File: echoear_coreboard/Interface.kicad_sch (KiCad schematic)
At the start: 0 parts

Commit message: Starting Interface SCH
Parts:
- added U2: (no value), symbol Symbols:1.0K-N-3PB
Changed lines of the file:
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@@
 	(generator_version "10.0")
 	(paper "A4")
+	(symbol
+		(lib_id "Symbols:1.0K-N-3PB")
+		(at 34.29 29.21 0)
+		(unit 1)
+		(body_style 1)
+		(exclude_from_sim no)
+		(in_bom yes)
+		(on_board yes)
+		(in_pos_files yes)
+		(dnp no)
+		(fields_autoplaced yes)
+		(property "Reference" "U2"
+			(at 45.72 38.0999 0)
+			(show_name no)
+			(do_not_autoplace no)
+			(effects
+				(font
+					(size 1.27 1.27)
+				)
+				(justify left)
+			)
+		)
+		(property "Value" ""
+			(at 34.29 29.21 0)
+			(show_name no)
+			(do_not_autoplace no)
+			(effects
+				(font
+					(size 1.27 1.27)
+				)
+			)
+		)
+		(property "Footprint" ""
+			(at 34.29 29.21 0)
+			(hide yes)
+			(show_name no)
+			(do_not_autoplace no)
+			(effects
+				(font
+					(size 1.27 1.27)
+				)
+			)
+		)
+		(property "Datasheet" ""
+			(at 34.29 29.21 0)
+			(hide yes)
+			(show_name no)
+			(do_not_autoplace no)
+			(effects
+				(font
+					(size 1.27 1.27)
+				)
+			)
+		)
+		(property "Description" ""
+			(at 34.29 29.21 0)
+			(hide yes)
+			(show_name no)
+			(do_not_autoplace no)
+			(effects
+				(font
+					(size 1.27 1.27)
+				)
+			)
+		)
+		(pin ""
+		)
+		(pin ""
+		)
+		(pin ""
+		)
+		(pin ""
+		)
+		(pin ""
+		)
+		(instances
+			(project "echoear_coreboard"
+				(path "/919b249b-28e6-49d6-a46c-47b0cfe0d5d1/25b0c935-1253-4e1a-a7e3-572f314d3e73"
+					(reference "U2")
+					(unit 1)
+				)
+			)
+		)
+	)
 )

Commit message: Finished touch schematic
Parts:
- added CN1: HC-1.25-2PLT, Library:CONN-SMD_HC-1.25-2PLT, symbol Sym_easyeda2kicad:HC-1.25-2PLT
- U2: value (none) -> 1.0K-N-3PB; footprint (none) -> Library:FPC-SMD_3P-P1.00_HDGC_1.0K-N-3PB; LCSC (none) -> C2915549
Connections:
- net TOUCH: now reaches U2. (4)
- net TOUCH: now also CN1.1, CN1.2
- new net GND: CN1.3, CN1.4, U2. (4)
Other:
- note added: "TOUCH"
- moved on the sheet: U2

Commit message: First draft of Interface SCH
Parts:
- added C4: 10u, Capacitor_SMD:C_0603_1608Metric, symbol Device:C
- added C5, C6: 100n, Capacitor_SMD:C_0402_1005Metric, symbol Device:C
- added CN2: HC-1.25-2PLT, easyeda2kicad:CONN-SMD_HC-1.25-2PLT, symbol Sym_easyeda2kicad:HC-1.25-2PLT
- added CN3: YXT-BB10-24S-02, easyeda2kicad:CONN-SMD_YXT-BB10-24S-02, symbol Sym_easyeda2kicad:YXT-BB10-24S-02
- added H1, H2: ZX-PZ1.27-2-4PWZ, easyeda2kicad:HDR-SMD_8P-P1.27-LS5.5_ZX-PZ1.27-2-4PWZ, symbol Symbols:ZX-PZ1.27-2-4PWZ
- added Q1: AO3401A, Package_TO_SOT_SMD:SOT-23, symbol Transistor_FET:AO3401A
- added Q2: AO3400A, Package_TO_SOT_SMD:SOT-23, symbol Transistor_FET:AO3400A
- added R4: 20 ohms, Resistor_SMD:R_0402_1005Metric, symbol Device:R
- added R5: 10k, Resistor_SMD:R_0402_1005Metric, symbol Device:R
- added U2: 8.03A0.039200, easyeda2kicad:FPC-SMD_39P-P0.60_DIANWEI_8.03A0.039200, symbol Sym_easyeda2kicad:8.03A0.039200
- added U3: BMI270, easyeda2kicad:LGA-14_L3.0-W2.5-P0.50-BR, symbol Sym_easyeda2kicad:BMI270
- renumbered U2 to FPC1
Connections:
- net GND: now also C4.1, C5.1, C6.2, CN2.1, CN2.3, CN2.4, CN3.11, CN3.15, CN3.17, CN3.19, CN3.25, CN3.26, CN3.27, CN3.28, CN3.3, CN3.8, H1.1, Q2.2 (S), R5.2, U2.1, U2.20, U2.27, U2.30, U2.33, U2.36, U2.39, U2.40, U2.41, U2.7, U2.9, U3.1 (SDO), U3.6 (GNDIO), U3.7 (GND)
- new net: Q2.3 (D), R4.2
- new net BAT_SCL: H1.4
- new net BAT_SDA: H1.2
- new net CHIP_PU: H2.3
- new net ESP_BOOT: H1.8
- new net ICM_INT1: U3.4 (INT1)
- new net ICM_SCL: U3.13 (SCX)
- new net ICM_SDA: U3.14 (SDX)
- new net LCD_BLK: Q2.1 (G), R5.1
- new net LCD_CS: CN3.24, U2.11
- new net LCD_DC: U2.8
- new net LCD_RST: CN3.12, CN3.6, U2.21, U2.4
- new net LCD_SCL: CN3.21, U2.10
- new net LCD_SDA0: CN3.23, U2.12
- new net LCD_SDA1: CN3.22, U2.13
- new net LCD_SDA2: CN3.18, U2.14
- new net LCD_SDA3: CN3.16, U2.15
- new net LCD_TE: CN3.13, U2.22
- new net LEDK: CN3.2, U2.38
- new net LED_K: R4.1
- new net MCU_3V3: C5.2, C6.1, CN3.9, H1.5, Q1.2 (S), U2.2, U3.12 (CSB), U3.5 (VDDIO), U3.8 (VDD)
- new net POWER_CTRL: H1.7, Q1.1 (G)
- new net SD_CLK: H2.5
- new net SD_CMD: H1.6
- new net SD_DA0: H2.7
- new net TP_INT: CN3.7, U2.3
- new net TP_SCL: CN3.4, U2.6
- new net TP_SDA: CN3.5, U2.5
- new net U1RXD: H2.1
- new net U1TXD: H2.4
- new net USB_DN: H2.6
- new net USB_DP: H2.8
- new net VBAT_IN: CN2.2, H1.3
- new net VCC_3V3: C4.2, CN3.1, CN3.10, Q1.3 (D), U2.25, U2.26, U2.28, U2.29, U2.37
- new net VIN: H2.2
- no-connect marks 0 -> 17
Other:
- note added: "B2B CONNECT"
- note added: "BAT CONNECT"
- note added: "IMU"
- note added: "LCD"
- moved on the sheet: CN1, FPC1

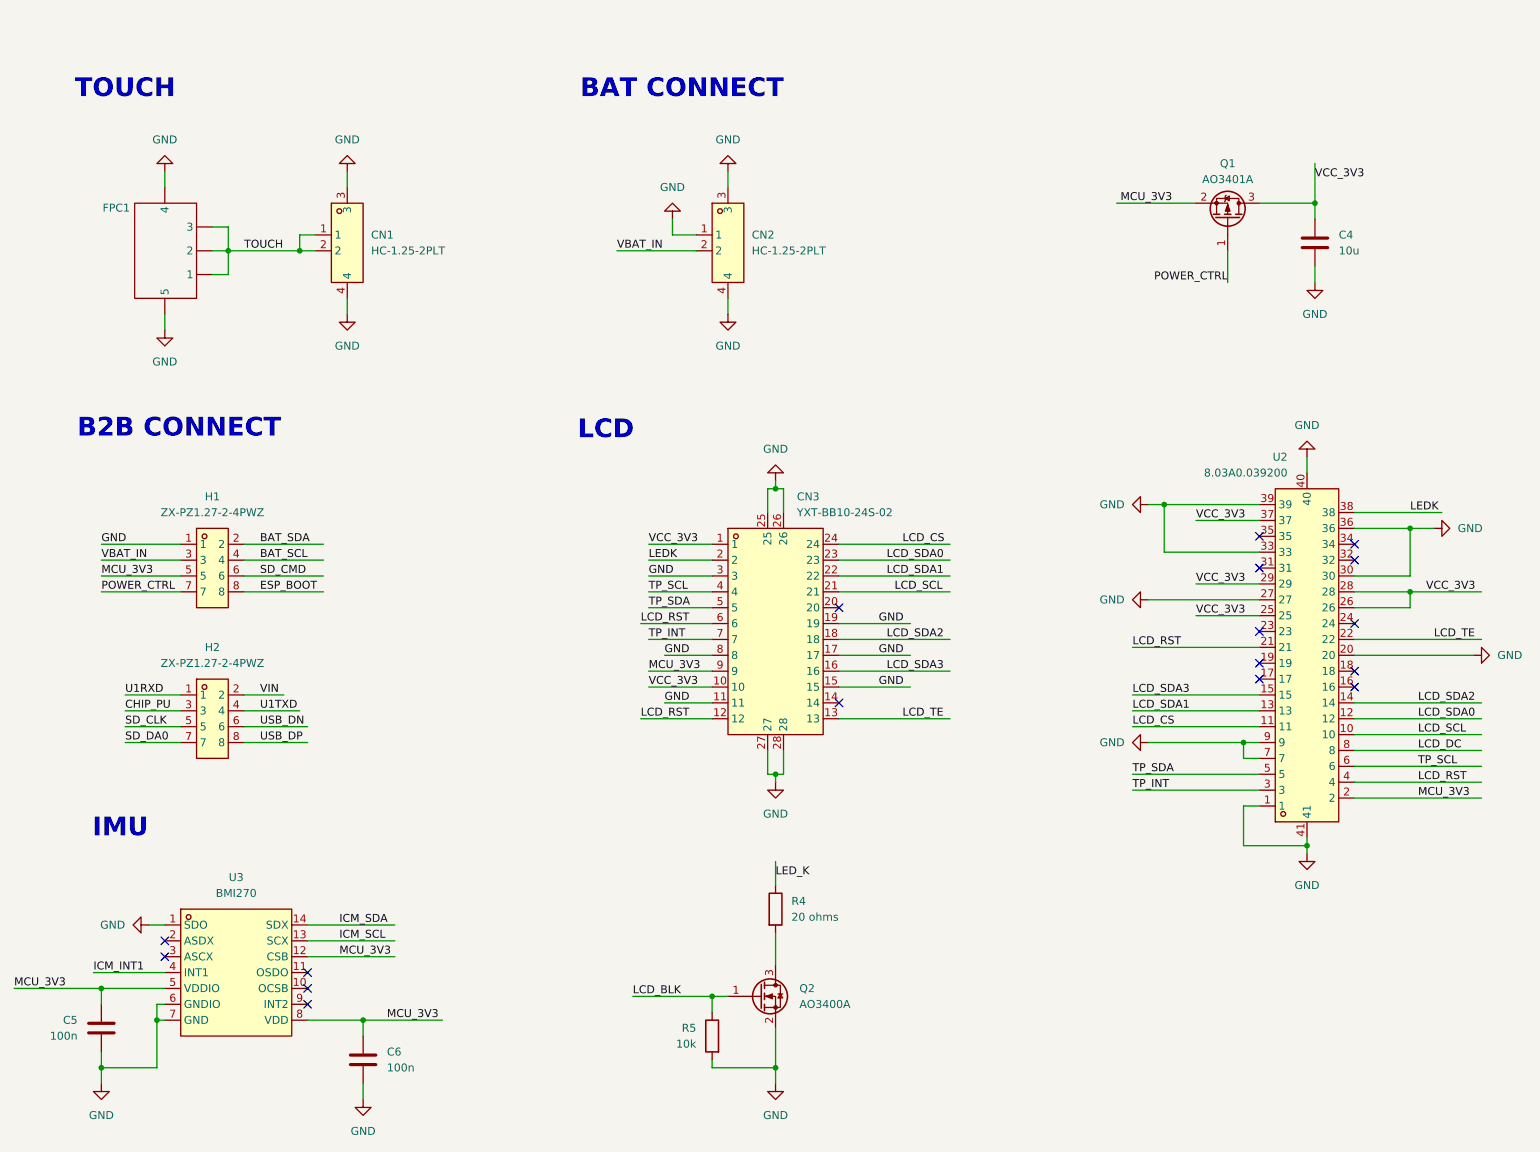
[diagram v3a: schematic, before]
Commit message: Fixed ERC errors for MCU/Interface SCH
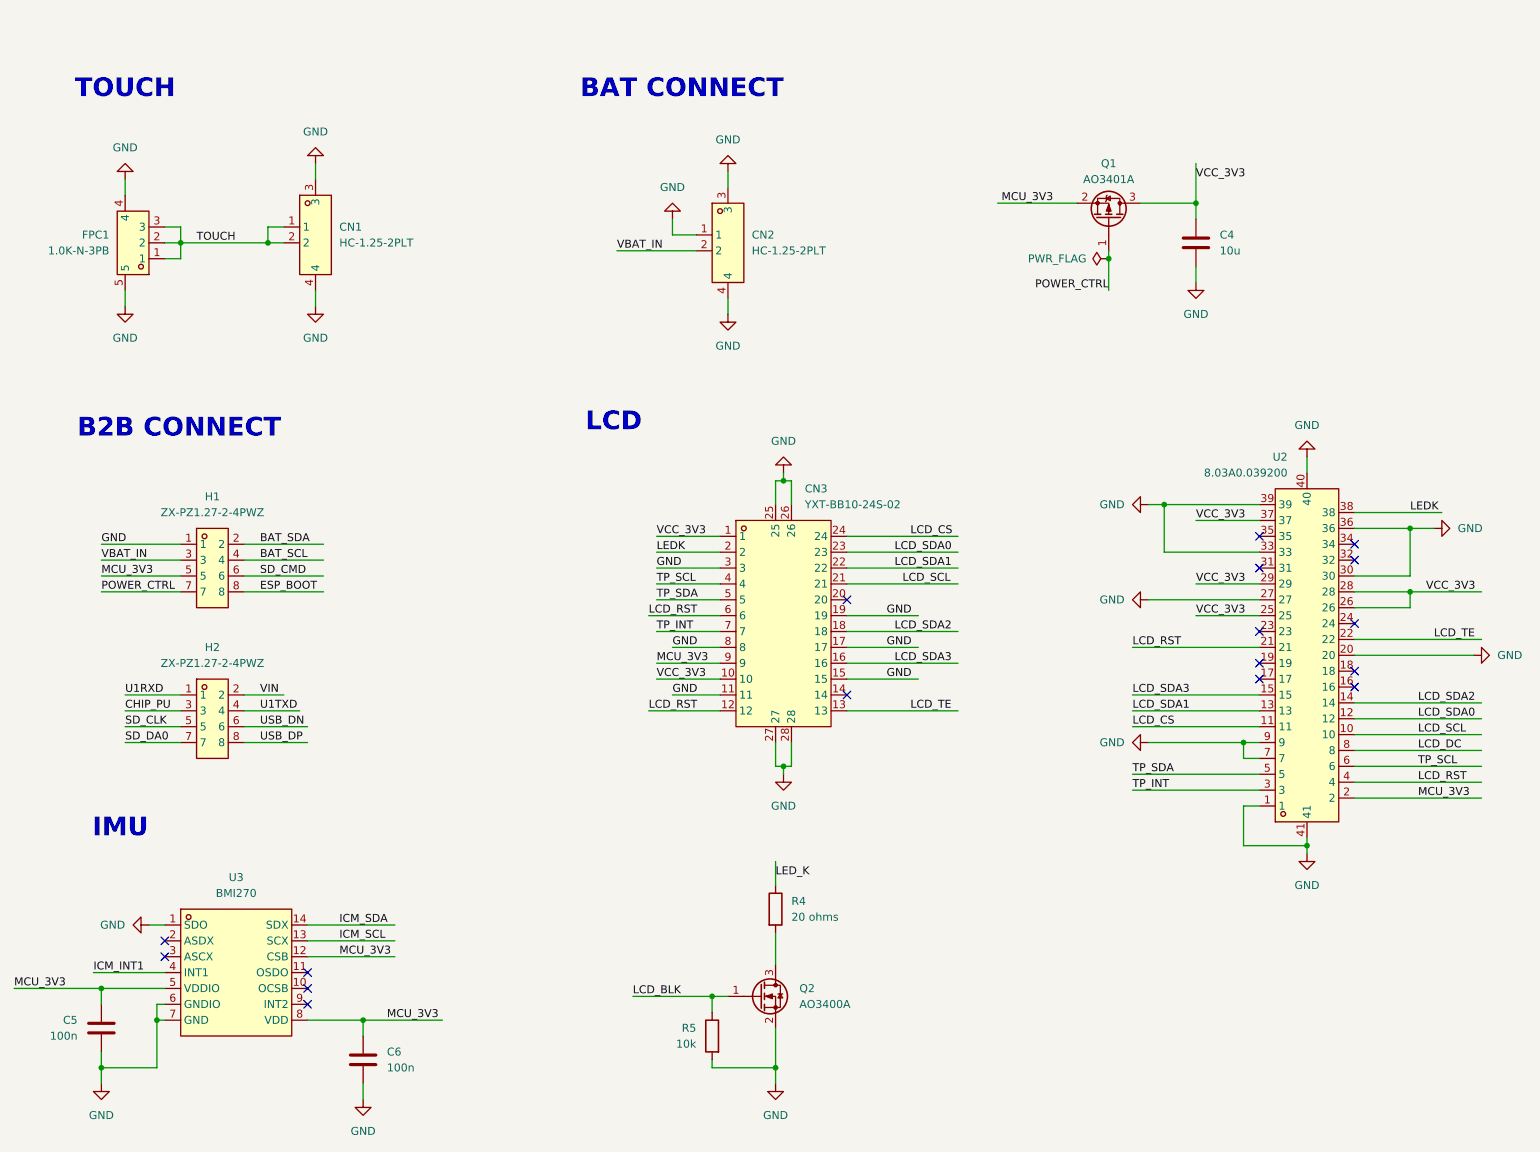
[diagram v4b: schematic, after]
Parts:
- removed FPC1: 1.0K-N-3PB, Library:FPC-SMD_3P-P1.00_HDGC_1.0K-N-3PB, symbol Symbols:1.0K-N-3PB
- added FPC1: 1.0K-N-3PB, easyeda2kicad:FPC-SMD_3P-P1.00_HDGC_1.0K-N-3PB, symbol Sym_easyeda2kicad:1.0K-N-3PB
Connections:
- net GND: now also FPC1.4, FPC1.5
- net TOUCH: now also FPC1.1, FPC1.2, FPC1.3
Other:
- moved on the sheet: C4, CN1, CN3, Q1

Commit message: Starting codec SCH
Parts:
- Q1: LCSC (none) -> C15127
- Q2: LCSC (none) -> C20917
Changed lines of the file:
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@@
+			)
+		)
+		(property "LCSC" "C15127"
+			(at 191.77 48.26 90)
+			(hide yes)
+			(show_name no)
+			(do_not_autoplace no)
+			(effects
+				(font
+					(size 1.27 1.27)
+				)
 			)
 		)
@@
 			(at 135.89 172.72 0)
 			(hide yes)
+			(show_name no)
+			(do_not_autoplace no)
+			(effects
+				(font
+					(size 1.27 1.27)
+				)
+			)
+		)
+		(property "LCSC" "C20917"
+			(at 135.89 172.72 0)
+			(hide yes)
